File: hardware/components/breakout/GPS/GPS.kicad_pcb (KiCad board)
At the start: 2 copper layers, 6 parts, among them J1 Conn_01x07_Pin, J2 Conn_01x07_Pin, U1 NEO-M9N

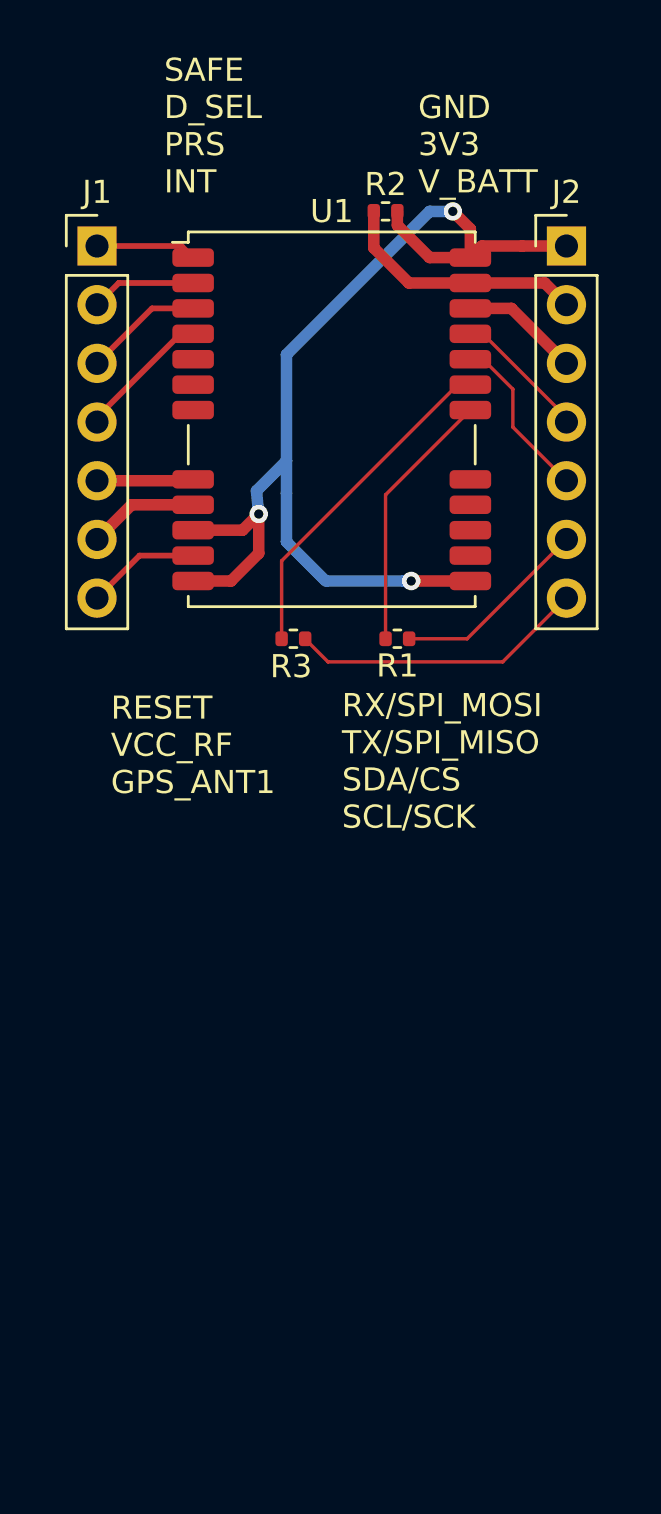
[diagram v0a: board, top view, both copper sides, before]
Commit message: GPS breakout board にアンテナを追加
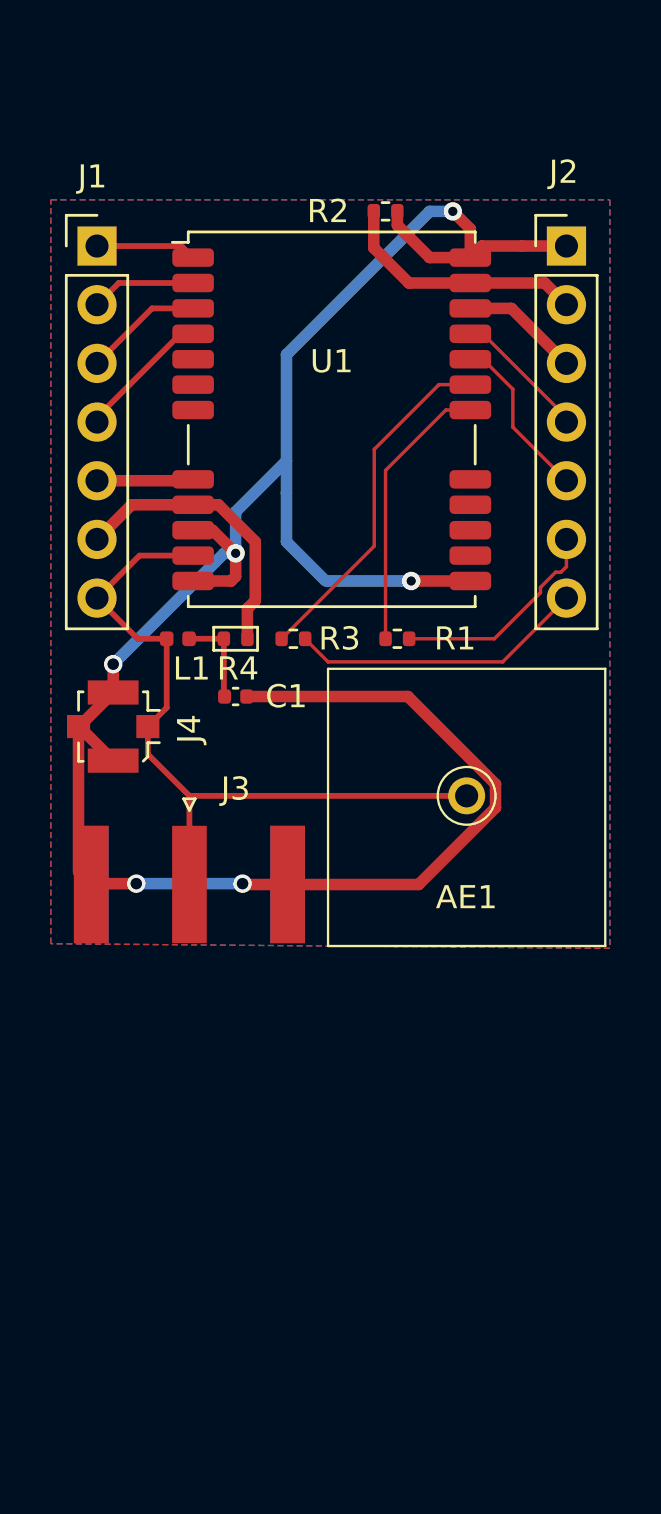
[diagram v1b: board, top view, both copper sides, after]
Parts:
- added AE1: Antenna, WOBCLibrary:GNSS_Antenna_1212, F.Cu at (136.0, 99.3)
- added C1: 100nF, Capacitor_SMD:C_0402_1005Metric, F.Cu at (126.0, 94.5)
- added J3: SMA, Connector_Coaxial:SMA_Amphenol_132289_EdgeMount, F.Cu at (124.0, 102.6)
- added J4: U.FL, Connector_Coaxial:U.FL_Molex_MCRF_73412-0110_Vertical, F.Cu at (120.7, 95.8)
- added L1: 27nH, 300mA, Inductor_SMD:L_0402_1005Metric, F.Cu at (123.5, 92.0)
- added R4: 10, PCM_Resistor_SMD_AKL:R_0402_1005Metric, F.Cu at (126.0, 92.0)
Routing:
- net GND: track 49.1 -> 101.0 mm, vias 3 -> 6
- net GPS_ANT1: track 4.92 -> 32.4 mm
- net VCC_RF: track 4.78 -> 12.5 mm
- net Net-(C1-Pad1): track 0.00 -> 4.02 mm
- net SDA/CS: track 8.59 -> 9.42 mm
- net Net-(U1-SDA/~{SPI_CS}): track 11.4 -> 12.0 mm
- added copper zone on B.Cu, net GND
- added copper zone on F.Cu, net GND

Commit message: ごちゃごちゃになったので一回コミットします。 GPSとLiPoとLoRaの一部が変化してると思います。
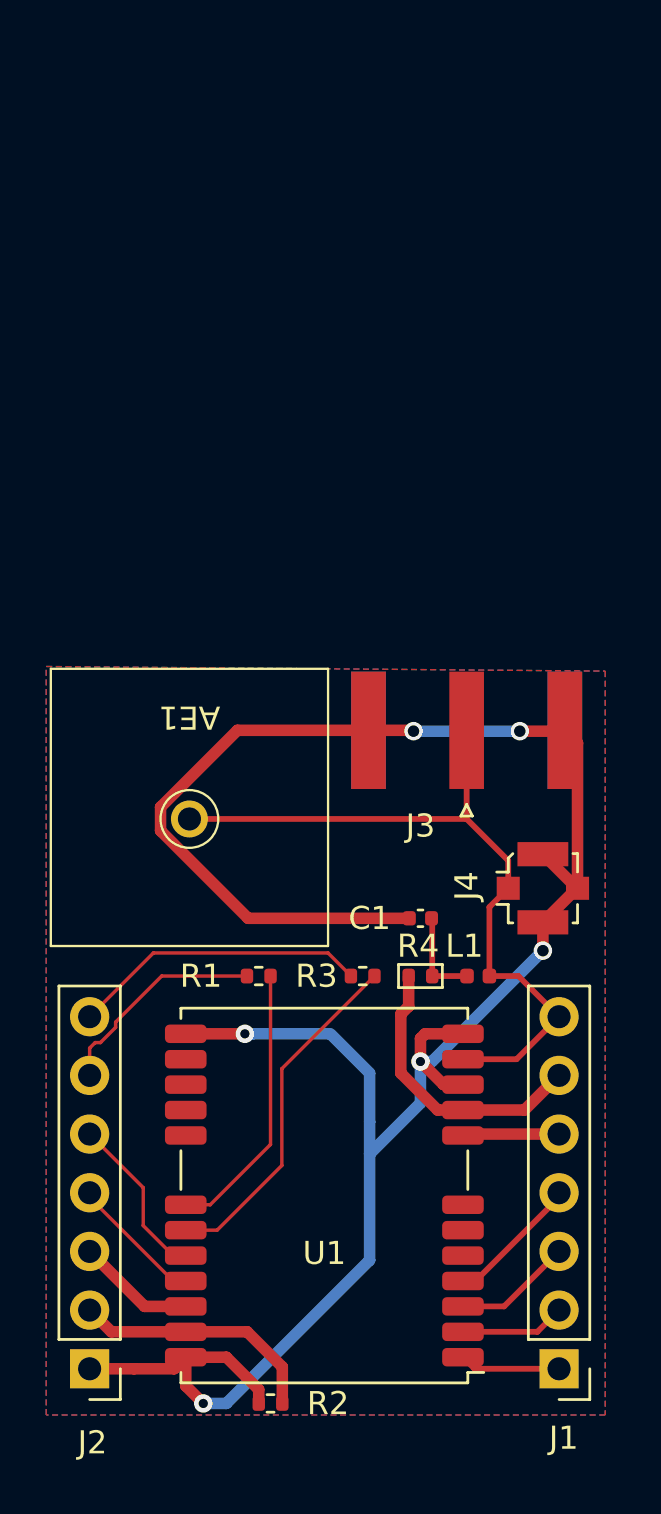
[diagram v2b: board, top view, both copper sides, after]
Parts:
- moved J2 52.8 mm to (119.7, 123.6), turned to 180 degrees
- moved J1 52.6 mm to (140.0, 123.6), turned to 180 degrees
- moved R2 51.8 mm to (127.5, 125.1), turned to 180 degrees
- moved U1 33.6 mm to (129.8, 116.1), turned to 180 degrees
- moved J4 19.9 mm to (139.3, 102.8), turned to -90 degrees
- moved L1 19.5 mm to (136.5, 106.6), turned to 180 degrees
- moved R4 16.6 mm to (134.0, 106.6), turned to 0 degrees
- moved R1 15.8 mm to (127.0, 106.6), turned to 0 degrees
- moved R3 14.9 mm to (131.5, 106.6), turned to 180 degrees
- moved J3 13.7 mm to (136.0, 96.0), turned to 90 degrees
- moved C1 12.5 mm to (134.0, 104.1), turned to 180 degrees
- moved AE1 12.0 mm to (124.0, 99.3), turned to 180 degrees

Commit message: RP2040・LiPo・LoRa・ModuleIF・LCDのLCSC割り当て完了しました．基板設計中に確認していただきたいです． 何点か変更があります．LiPoPowerSimpleの充放電ICのProg周辺の抵抗値がLiPoPowerと異なっていたので合わせてしまっています． 今，ModuleIFのロードセルが指定されていたものではJLCPCBに在庫がなく，同じシリーズの在庫が多少残っているものを登録してます．そのためフットプリントと整合してません．別の物使うか判断をお願いします．
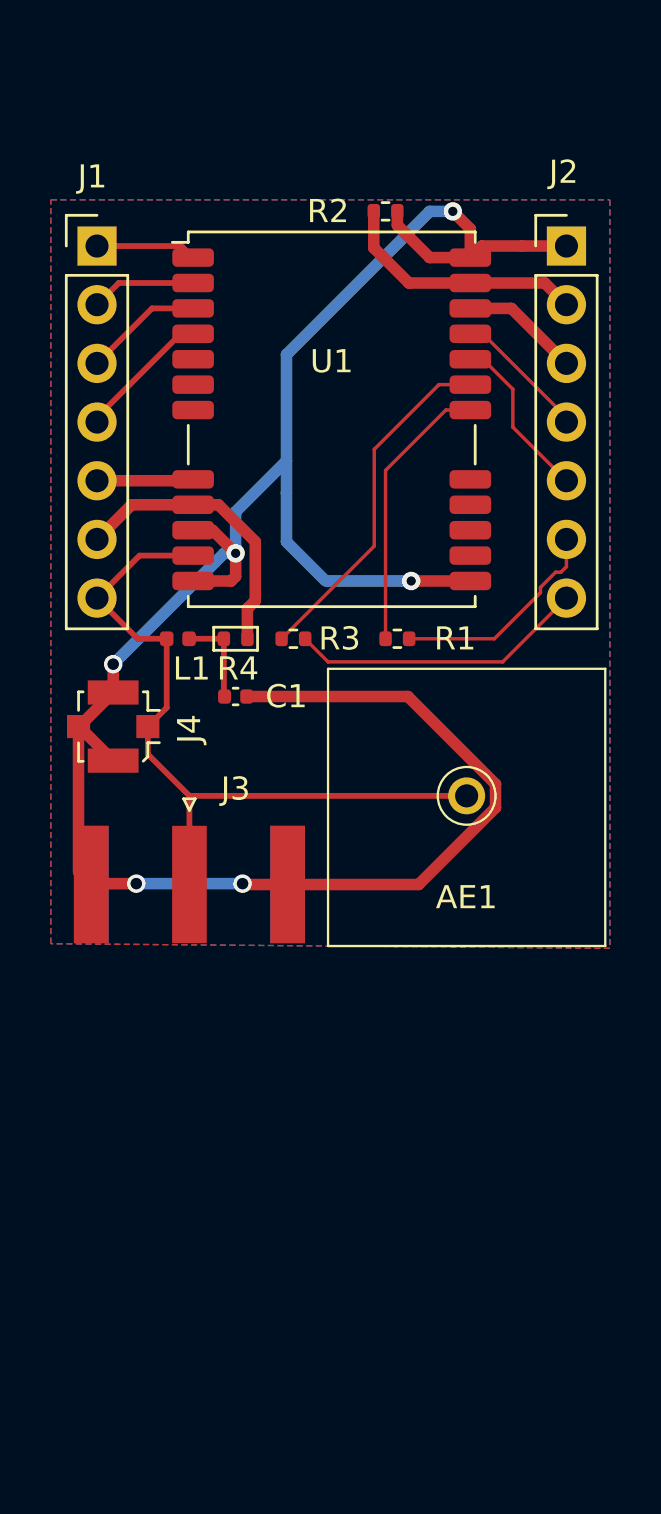
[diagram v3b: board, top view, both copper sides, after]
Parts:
- moved J2 52.8 mm to (140.3, 75.0), turned to 0 degrees
- moved J1 52.6 mm to (120.0, 75.0), turned to 0 degrees
- moved R2 51.8 mm to (132.5, 73.5), turned to 0 degrees
- moved U1 33.6 mm to (130.2, 82.5), turned to 0 degrees
- moved J4 19.9 mm to (120.7, 95.8), turned to 90 degrees
- moved L1 19.5 mm to (123.5, 92.0), turned to 0 degrees
- moved R4 16.6 mm to (126.0, 92.0), turned to 180 degrees
- moved R1 15.8 mm to (133.0, 92.0), turned to 180 degrees
- moved R3 14.9 mm to (128.5, 92.0), turned to 0 degrees
- moved J3 13.7 mm to (124.0, 102.6), turned to -90 degrees
- moved C1 12.5 mm to (126.0, 94.5), turned to 0 degrees
- moved AE1 12.0 mm to (136.0, 99.3), turned to 0 degrees
